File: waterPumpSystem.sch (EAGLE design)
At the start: 6 parts, among them Q1 2N2222A, X1 RASPI_BOARD_B+#_E4

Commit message: Schematic
made some changes
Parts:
- added U$1: NRF24L01, nrf24l01:NRF24L01
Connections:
- new net N$11: PCB1.8, U$1.CSN
- new net N$12: PCB1.7, U$1.CE
- new net N$13: PCB1.GND, U$1.VSS
- new net N$14: PCB1.3.3V, U$1.VDD
- new net N$15: PCB1.13, U$1.SCK
- new net N$16: PCB1.~11, U$1.MOSI
- new net N$17: PCB1.12, U$1.MISO
- net N$4: now also PCB1.5V; no longer PCB1.3.3V
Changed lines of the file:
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@@
 <part name="P+1" library="supply1" library_urn="urn:adsk.eagle:library:371" deviceset="+12V" device=""/>
 <part name="J_ULTRASONIC_1" library="Ultrasonic Sensor HC-SR04" deviceset="HC-SR04" device=""/>
+<part name="U$1" library="nrf24l01" deviceset="NRF24L01" device=""/>
 </parts>
 <sheets>
@@
 <instance part="P+1" gate="1" x="198.12" y="88.9"/>
 <instance part="J_ULTRASONIC_1" gate="J_ULTRASONIC" x="177.8" y="83.82" rot="R90"/>
+<instance part="U$1" gate="G$1" x="137.16" y="104.14"/>
 </instances>
 <busses>
@@
 </segment>
 </net>
-<net name="N$4" class="0">
-<segment>
-<pinref part="PCB1" gate="G$1" pin="3.3V"/>
-<wire x1="185.42" y1="27.94" x2="162.56" y2="27.94" width="0.1524" layer="91"/>
-<pinref part="J_ULTRASONIC_1" gate="J_ULTRASONIC" pin="5V"/>
-<wire x1="185.42" y1="27.94" x2="185.42" y2="71.12" width="0.1524" layer="91"/>
-</segment>
-</net>
 <net name="N$8" class="0">
 <segment>
@@
 </segment>
 </net>
+<net name="N$11" class="0">
+<segment>
+<pinref part="U$1" gate="G$1" pin="CSN"/>
+<wire x1="152.4" y1="96.52" x2="157.48" y2="96.52" width="0.1524" layer="91"/>
+<wire x1="157.48" y1="96.52" x2="157.48" y2="66.04" width="0.1524" layer="91"/>
+<wire x1="157.48" y1="66.04" x2="116.84" y2="66.04" width="0.1524" layer="91"/>
+<wire x1="116.84" y1="66.04" x2="116.84" y2="33.02" width="0.1524" layer="91"/>
+<pinref part="PCB1" gate="G$1" pin="8"/>
+<wire x1="116.84" y1="33.02" x2="119.38" y2="33.02" width="0.1524" layer="91"/>
+</segment>
+</net>
+<net name="N$12" class="0">
+<segment>
+<pinref part="U$1" gate="G$1" pin="CE"/>
+<wire x1="152.4" y1="99.06" x2="154.94" y2="99.06" width="0.1524" layer="91"/>
+<wire x1="154.94" y1="99.06" x2="154.94" y2="68.58" width="0.1524" layer="91"/>
+<wire x1="154.94" y1="68.58" x2="114.3" y2="68.58" width="0.1524" layer="91"/>
+<wire x1="114.3" y1="68.58" x2="114.3" y2="40.64" width="0.1524" layer="91"/>
+<pinref part="PCB1" gate="G$1" pin="7"/>
+<wire x1="114.3" y1="40.64" x2="119.38" y2="40.64" width="0.1524" layer="91"/>
+</segment>
+</net>
+<net name="N$13" class="0">
+<segment>
+<pinref part="U$1" gate="G$1" pin="VSS"/>
+<wire x1="119.38" y1="91.44" x2="111.76" y2="91.44" width="0.1524" layer="91"/>
+<wire x1="111.76" y1="91.44" x2="111.76" y2="17.78" width="0.1524" layer="91"/>
+<pinref part="PCB1" gate="G$1" pin="GND"/>
+<wire x1="111.76" y1="17.78" x2="119.38" y2="17.78" width="0.1524" layer="91"/>
+</segment>
+</net>
+<net name="N$4" class="0">
+<segment>
+<pinref part="PCB1" gate="G$1" pin="5V"/>
+<pinref part="J_ULTRASONIC_1" gate="J_ULTRASONIC" pin="5V"/>
+<wire x1="162.56" y1="30.48" x2="185.42" y2="30.48" width="0.1524" layer="91"/>
+<wire x1="185.42" y1="30.48" x2="185.42" y2="71.12" width="0.1524" layer="91"/>
+</segment>
+</net>
+<net name="N$14" class="0">
+<segment>
+<pinref part="U$1" gate="G$1" pin="VDD"/>
+<wire x1="119.38" y1="104.14" x2="116.84" y2="104.14" width="0.1524" layer="91"/>
+<wire x1="116.84" y1="104.14" x2="116.84" y2="71.12" width="0.1524" layer="91"/>
+<wire x1="116.84" y1="71.12" x2="167.64" y2="71.12" width="0.1524" layer="91"/>
+<wire x1="167.64" y1="71.12" x2="167.64" y2="27.94" width="0.1524" layer="91"/>
+<pinref part="PCB1" gate="G$1" pin="3.3V"/>
+<wire x1="167.64" y1="27.94" x2="162.56" y2="27.94" width="0.1524" layer="91"/>
+</segment>
+</net>
+<net name="N$15" class="0">
+<segment>
+<pinref part="U$1" gate="G$1" pin="SCK"/>
+<wire x1="152.4" y1="93.98" x2="160.02" y2="93.98" width="0.1524" layer="91"/>
+<wire x1="160.02" y1="93.98" x2="160.02" y2="73.66" width="0.1524" layer="91"/>
+<wire x1="160.02" y1="73.66" x2="109.22" y2="73.66" width="0.1524" layer="91"/>
+<wire x1="109.22" y1="73.66" x2="109.22" y2="20.32" width="0.1524" layer="91"/>
+<pinref part="PCB1" gate="G$1" pin="13"/>
+<wire x1="109.22" y1="20.32" x2="119.38" y2="20.32" width="0.1524" layer="91"/>
+</segment>
+</net>
+<net name="N$16" class="0">
+<segment>
+<pinref part="U$1" gate="G$1" pin="MOSI"/>
+<wire x1="152.4" y1="91.44" x2="162.56" y2="91.44" width="0.1524" layer="91"/>
+<wire x1="162.56" y1="91.44" x2="162.56" y2="76.2" width="0.1524" layer="91"/>
+<wire x1="162.56" y1="76.2" x2="106.68" y2="76.2" width="0.1524" layer="91"/>
+<wire x1="106.68" y1="76.2" x2="106.68" y2="25.4" width="0.1524" layer="91"/>
+<pinref part="PCB1" gate="G$1" pin="~11"/>
+<wire x1="106.68" y1="25.4" x2="119.38" y2="25.4" width="0.1524" layer="91"/>
+</segment>
+</net>
+<net name="N$17" class="0">
+<segment>
+<pinref part="U$1" gate="G$1" pin="MISO"/>
+<wire x1="152.4" y1="88.9" x2="152.4" y2="78.74" width="0.1524" layer="91"/>
+<wire x1="152.4" y1="78.74" x2="104.14" y2="78.74" width="0.1524" layer="91"/>
+<wire x1="104.14" y1="78.74" x2="104.14" y2="22.86" width="0.1524" layer="91"/>
+<pinref part="PCB1" gate="G$1" pin="12"/>
+<wire x1="104.14" y1="22.86" x2="119.38" y2="22.86" width="0.1524" layer="91"/>
+</segment>
+</net>

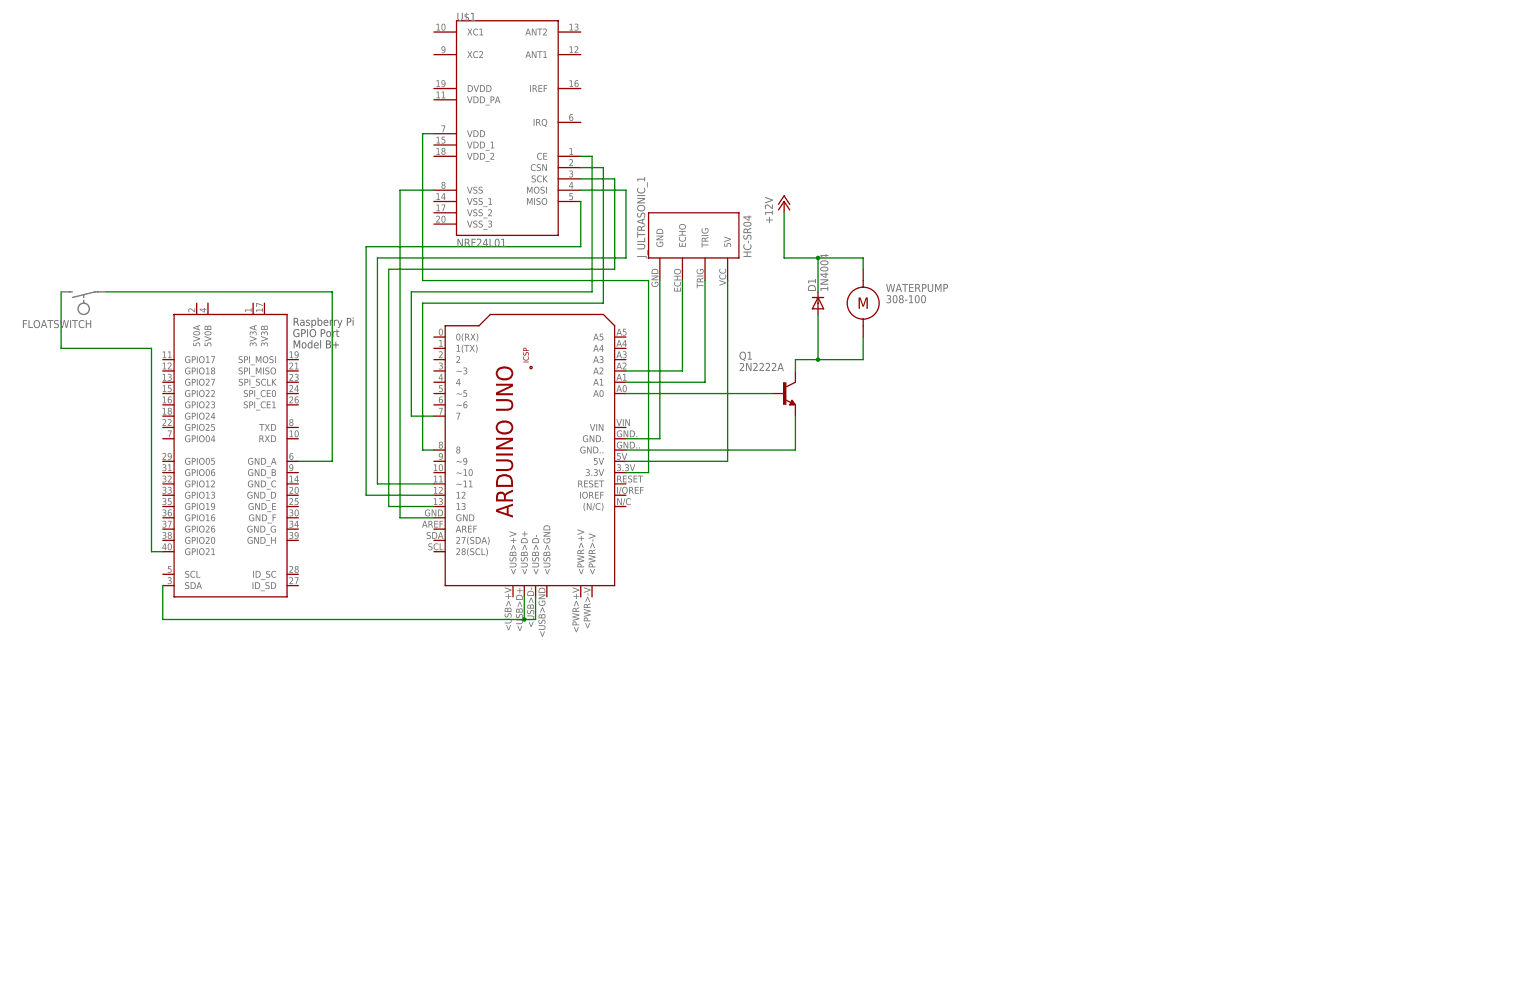
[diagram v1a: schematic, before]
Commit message: Add files via upload
add two arduinos, two lcds, photocell, moisture sensor, humidity sensor
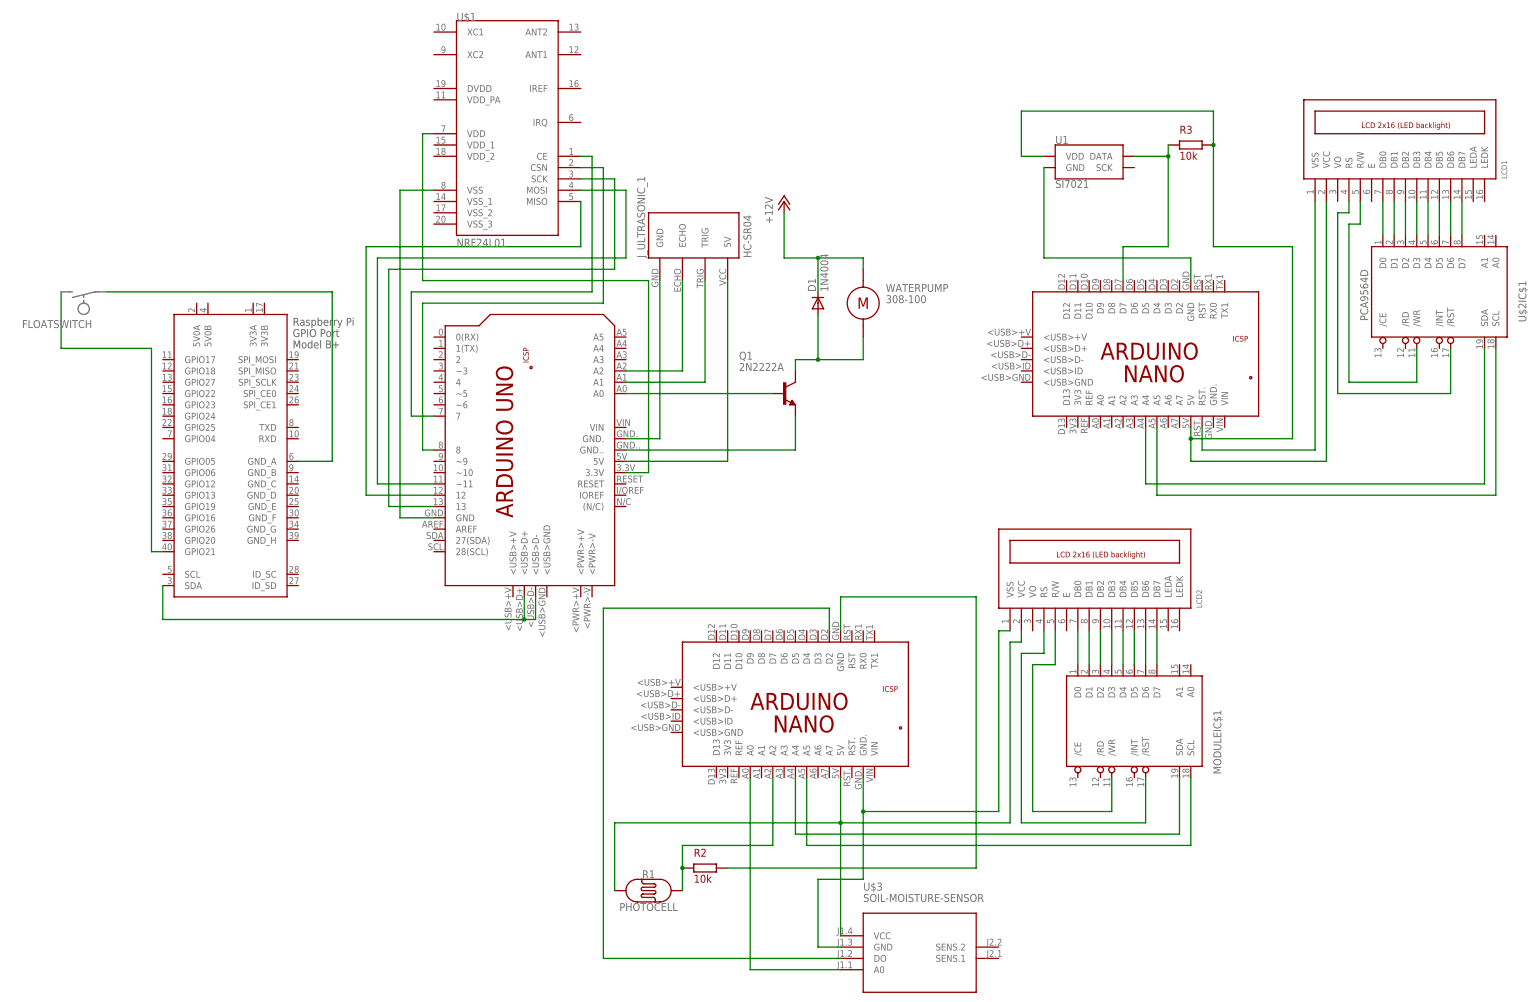
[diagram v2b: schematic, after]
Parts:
- added LCD1, LCD2: LCD_2X16_SIL, lcd_2x16_led_backlight:LCD_2X16_SIL
- added MODULE, U$2: PCA9564D, i2c:PCA9564D
- added PCB2, PCB3: ARDUINO_NANO, Arduino_revC:ARDUINO_NANO
- added R1: PHOTOCELL, SparkFun-Sensors:PHOTOCELLPTH
- added R2, R3: 10k, ngspice-simulation:R
- added U$3: SOIL-MOISTURE-SENSOR, diy-modules:SOIL-MOISTURE-SENSOR
- added U1: SI7021, SparkFun-Sensors:SI7021
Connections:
- new net N$18: PCB2.GND, U1.GND
- new net N$19: LCD1.R/W, U$2IC$1./WR
- new net N$20: LCD1.DB0, U$2IC$1.D0
- new net N$21: PCB2.D7, R3.1, U1.DATA
- new net N$22: LCD1.DB1, U$2IC$1.D1
- new net N$23: LCD1.DB2, U$2IC$1.D2
- new net N$24: LCD1.DB3, U$2IC$1.D3
- new net N$25: LCD1.DB4, U$2IC$1.D4
- new net N$26: LCD1.DB5, U$2IC$1.D5
- new net N$27: LCD1.DB6, U$2IC$1.D6
- new net N$28: LCD1.DB7, U$2IC$1.D7
- new net N$29: LCD1.VSS, PCB2.RST.
- new net N$30: LCD1.VCC, PCB2.5V, R3.2, U1.VDD
- new net N$31: LCD1.RS, U$2IC$1./RST
- new net N$32: PCB2.A4, U$2IC$1.SDA
- new net N$33: PCB2.A5, U$2IC$1.SCL
- new net N$34: LCD2.DB0, MODULEIC$1.D0
- new net N$35: LCD2.DB1, MODULEIC$1.D1
- new net N$36: LCD2.DB2, MODULEIC$1.D2
- new net N$37: LCD2.DB3, MODULEIC$1.D3
- new net N$38: LCD2.DB4, MODULEIC$1.D4
- new net N$39: LCD2.DB5, MODULEIC$1.D5
- new net N$40: LCD2.DB6, MODULEIC$1.D6
- new net N$41: LCD2.DB7, MODULEIC$1.D7
- new net N$42: LCD2.R/W, MODULEIC$1./WR
- new net N$43: LCD2.RS, MODULEIC$1./RST
- new net N$44: MODULEIC$1.SDA, PCB3.A4
- new net N$45: MODULEIC$1.SCL, PCB3.A5
- new net N$46: LCD2.VCC, PCB3.5V, R1.P$1, U$3.VCC
- new net N$47: LCD2.VSS, PCB3.GND., U$3.GND
- new net N$48: PCB3.A2, R1.P$2, R2.1
- new net N$49: PCB3.GND, R2.2
- new net N$50: PCB3.A0, U$3.A0
- new net N$51: PCB3.D2, U$3.DO
